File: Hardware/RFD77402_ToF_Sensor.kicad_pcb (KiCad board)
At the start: 2 copper layers, 25.4 x 25.4 mm, 22 parts, among them J1 QWIIC_CONNECTORJS-1MM, J2 QWIIC_CONNECTORJS-1MM, J3 CONN_01, J4 I2C_STANDARD, U1 RFD77402, U4 CC_LICENSE

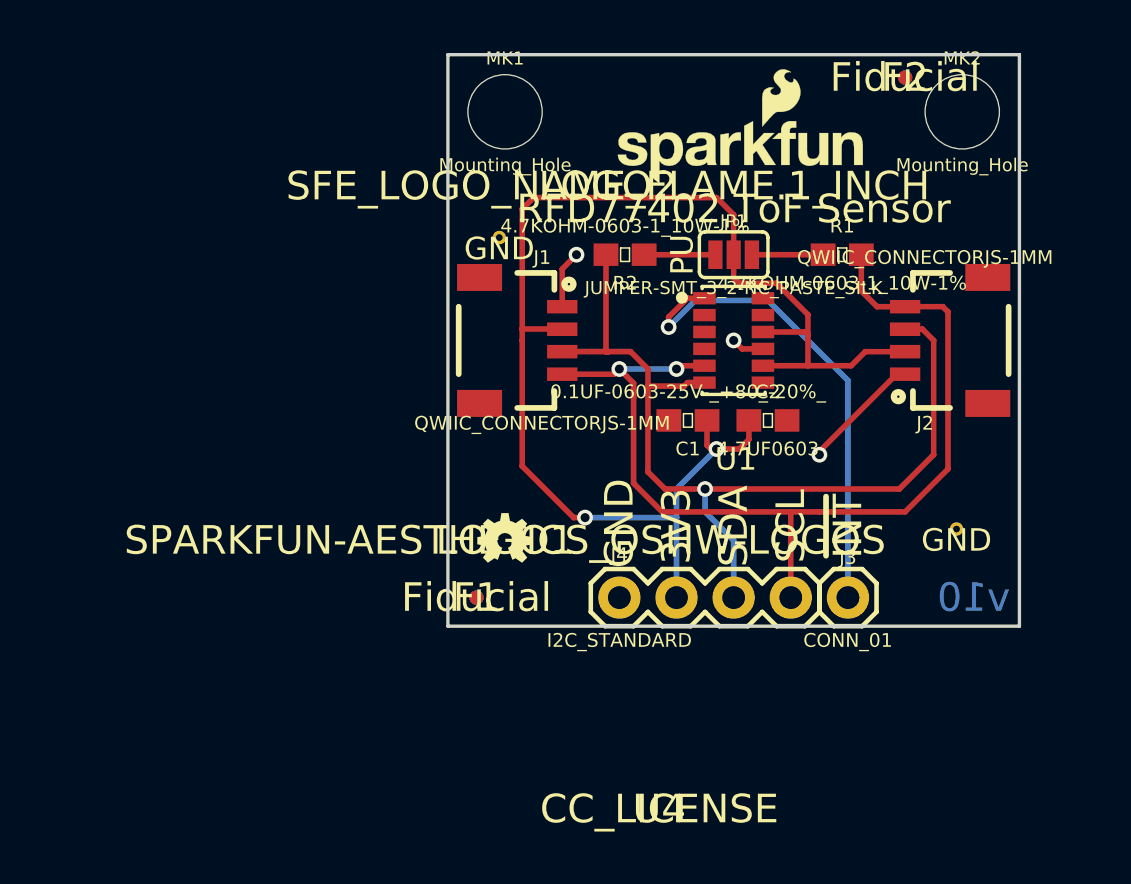
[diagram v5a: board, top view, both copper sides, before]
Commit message: fixed paste issue with fiducial
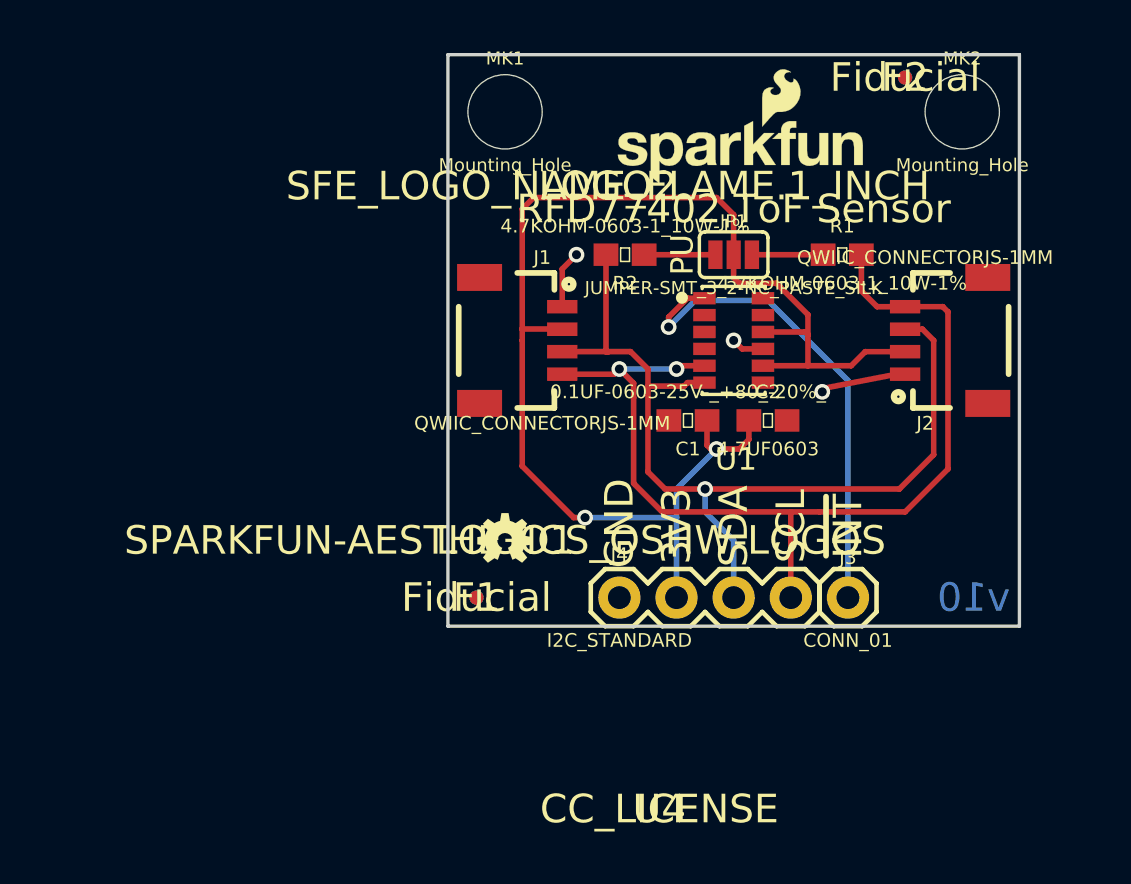
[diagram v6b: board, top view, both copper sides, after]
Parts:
- removed GND (x2): VIA-15mil, Hardware:VIA-15mil
- F1, F2, F3, F4: footprint Aesthetics:FIDUCIAL-MICRO -> Aesthetics:FIDUCIAL-MICRO-NO_PASTE
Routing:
- net GND: track 9.41 -> 7.92 mm
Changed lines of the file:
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@@
 (kicad_pcb (version 4) (host pcbnew 4.0.7)
   (general
-    (links 26)
+    (links 24)
     (no_connects 0)
-    (area 117.656001 84.328 173.827142 126.4622)
+    (area 137.084999 91.364999 162.635001 116.915001)
     (thickness 1.6)
     (drawings 23)
     (tracks 100)
     (zones 0)
-    (modules 22)
+    (modules 20)
     (nets 8)
   )
@@
       (net 1 GND) (solder_mask_margin 0.1016))
   )
-  (module Aesthetics:FIDUCIAL-MICRO (layer F.Cu)
-    (at 138.43 115.57)
-    (descr "FIDUCIAL - CIRCLE, 0.25IN")
-    (tags "FIDUCIAL - CIRCLE, 0.25IN")
-    (attr smd)
-    (fp_text reference F1 (at 0 0) (layer F.SilkS)
-      (effects (font (thickness 0.15)))
-    )
-    (fp_text value Fiducial (at 0 0) (layer F.SilkS)
-      (effects (font (thickness 0.15)))
-    )
-    (pad 1 smd circle (at 0 0) (size 0.635 0.635) (layers F.Cu F.Paste F.Mask)
-      (solder_mask_margin 0.1016))
-  )
-  (module Aesthetics:FIDUCIAL-MICRO (layer F.Cu)
-    (at 157.48 92.456)
-    (descr "FIDUCIAL - CIRCLE, 0.25IN")
-    (tags "FIDUCIAL - CIRCLE, 0.25IN")
-    (attr smd)
-    (fp_text reference F2 (at 0 0) (layer F.SilkS)
-      (effects (font (thickness 0.15)))
-    )
-    (fp_text value Fiducial (at 0 0) (layer F.SilkS)
-      (effects (font (thickness 0.15)))
-    )
-    (pad 1 smd circle (at 0 0) (size 0.635 0.635) (layers F.Cu F.Paste F.Mask)
-      (solder_mask_margin 0.1016))
-  )
   (module Connectors:1X04_1MM_RA (layer F.Cu)
     (at 157.48 104.14 90)
@@
       (net 1 GND))
   )
-  (module Aesthetics:FIDUCIAL-MICRO (layer B.Cu)
+  (module Aesthetics:FIDUCIAL-MICRO-NO_PASTE (layer F.Cu)
+    (at 138.43 115.57)
+    (descr "FIDUCIAL - CIRCLE, 0.25IN")
+    (tags "FIDUCIAL - CIRCLE, 0.25IN")
+    (attr smd)
+    (fp_text reference F1 (at 0 0) (layer F.SilkS)
+      (effects (font (thickness 0.15)))
+    )
+    (fp_text value Fiducial (at 0 0) (layer F.SilkS)
+      (effects (font (thickness 0.15)))
+    )
+    (pad 1 smd circle (at 0 0) (size 0.635 0.635) (layers F.Cu F.Mask)
+      (solder_mask_margin 0.1016))
+  )
+  (module Aesthetics:FIDUCIAL-MICRO-NO_PASTE (layer F.Cu)
+    (at 157.48 92.456)
+    (descr "FIDUCIAL - CIRCLE, 0.25IN")
+    (tags "FIDUCIAL - CIRCLE, 0.25IN")
+    (attr smd)
+    (fp_text reference F2 (at 0 0) (layer F.SilkS)
+      (effects (font (thickness 0.15)))
+    )
+    (fp_text value Fiducial (at 0 0) (layer F.SilkS)
+      (effects (font (thickness 0.15)))
+    )
+    (pad 1 smd circle (at 0 0) (size 0.635 0.635) (layers F.Cu F.Mask)
+      (solder_mask_margin 0.1016))
+  )
+  (module Aesthetics:FIDUCIAL-MICRO-NO_PASTE (layer B.Cu)
     (at 138.43 115.57)
     (descr "FIDUCIAL - CIRCLE, 0.25IN")
@@
       (effects (font (thickness 0.15)) (justify mirror))
     )
-    (pad 1 smd circle (at 0 0) (size 0.635 0.635) (layers B.Cu B.Paste B.Mask)
+    (pad 1 smd circle (at 0 0) (size 0.635 0.635) (layers B.Cu B.Mask)
       (solder_mask_margin 0.1016))
   )
-  (module Aesthetics:FIDUCIAL-MICRO (layer B.Cu)
+  (module Aesthetics:FIDUCIAL-MICRO-NO_PASTE (layer B.Cu)
     (at 157.48 92.456)
     (descr "FIDUCIAL - CIRCLE, 0.25IN")
@@
       (effects (font (thickness 0.15)) (justify mirror))
     )
-    (pad 1 smd circle (at 0 0) (size 0.635 0.635) (layers B.Cu B.Paste B.Mask)
+    (pad 1 smd circle (at 0 0) (size 0.635 0.635) (layers B.Cu B.Mask)
       (solder_mask_margin 0.1016))
-  )
-  (module Hardware:VIA-15mil (layer F.Cu)
-    (at 159.766 112.522)
-    (fp_text reference GND (at 0 0.5) (layer F.SilkS)
-      (effects (font (size 1 1) (thickness 0.15)))
-    )
-    (fp_text value VIA-15mil (at 0 -0.5) (layer F.Fab)
-      (effects (font (size 1 1) (thickness 0.15)))
-    )
-    (pad 1 thru_hole circle (at 0 0) (size 0.6 0.6) (drill 0.3) (layers *.Cu)
-      (net 1 GND) (zone_connect 2))
-  )
-  (module Hardware:VIA-15mil (layer F.Cu)
-    (at 139.446 99.568)
-    (fp_text reference GND (at 0 0.5) (layer F.SilkS)
-      (effects (font (size 1 1) (thickness 0.15)))
-    )
-    (fp_text value VIA-15mil (at 0 -0.5) (layer F.Fab)
-      (effects (font (size 1 1) (thickness 0.15)))
-    )
-    (pad 1 thru_hole circle (at 0 0) (size 0.6 0.6) (drill 0.3) (layers *.Cu)
-      (net 1 GND) (zone_connect 2))
   )
   (gr_text I2C-0x4C (at 149.86 106.68) (layer B.SilkS)
@@
   (gr_line (start 137.16 91.44) (end 162.56 91.44) (angle 90) (layer Edge.Cuts) (width 0.15))
   (gr_line (start 137.16 116.84) (end 137.16 91.44) (angle 90) (layer Edge.Cuts) (width 0.15))
+  (segment (start 153.797 106.281) (end 153.797 106.426) (width 0.25) (layer F.Cu) (net 1))
+  (segment (start 157.105 105.64) (end 153.797 106.281) (width 0.25) (layer F.Cu) (net 1))
+  (via (at 153.797 106.426) (size 0.7) (drill 0.4) (layers F.Cu B.Cu) (net 1))
   (segment (start 142.24 100.965) (end 142.24 102.64) (width 0.25) (layer F.Cu) (net 1))
   (via (at 142.875 100.33) (size 0.7) (drill 0.4) (layers F.Cu B.Cu) (net 1))
   (segment (start 142.24 100.965) (end 142.875 100.33) (width 0.25) (layer F.Cu) (net 1))
-  (segment (start 153.67 109.075) (end 153.67 109.22) (width 0.25) (layer F.Cu) (net 1))
-  (via (at 153.67 109.22) (size 0.7) (drill 0.4) (layers F.Cu B.Cu) (net 1))
-  (segment (start 157.105 105.64) (end 153.67 109.075) (width 0.25) (layer F.Cu) (net 1))
   (segment (start 157.48 105.64) (end 157.105 105.64) (width 0.25) (layer F.Cu) (net 1))
   (segment (start 151.16 104.515) (end 150.235 104.515) (width 0.25) (layer F.Cu) (net 1))
